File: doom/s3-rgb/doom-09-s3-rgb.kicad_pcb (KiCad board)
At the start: 4 copper layers, 182 x 80 mm, 100 parts, among them J1 54132-4062, J5 S2B-PH-K-S(LF)(SN), J6 S2B-PH-K-S(LF)(SN), Q1 AO3401A, Q2 FS8205A, SW1 PTS645SM43SMTR92 LFS, SW10 PTS645SM43SMTR92 LFS, SW11 MSK12C02, SW12 PTS645SM43SMTR92 LFS, SW13 PTS645SM43SMTR92 LFS, SW2 PTS645SM43SMTR92 LFS, SW3 PTS645SM43SMTR92 LFS, SW4 PTS645SM43SMTR92 LFS, SW5 PTS645SM43SMTR92 LFS, SW6 PTS645SM43SMTR92 LFS, SW7 PTS645SM43SMTR92 LFS, SW8 PTS645SM43SMTR92 LFS, SW9 PTS645SM43SMTR92 LFS, U1 ESP32-S3-WROOM-1-N16R8, U2 DW01A, U3 MCP23017-E/SO, U4 PCM5102APWR, U5 PAM8403DR, U6 TLV75533PDBVR, U7 BQ24075RGTR, U8 MT3608, U9 ESD 2-line

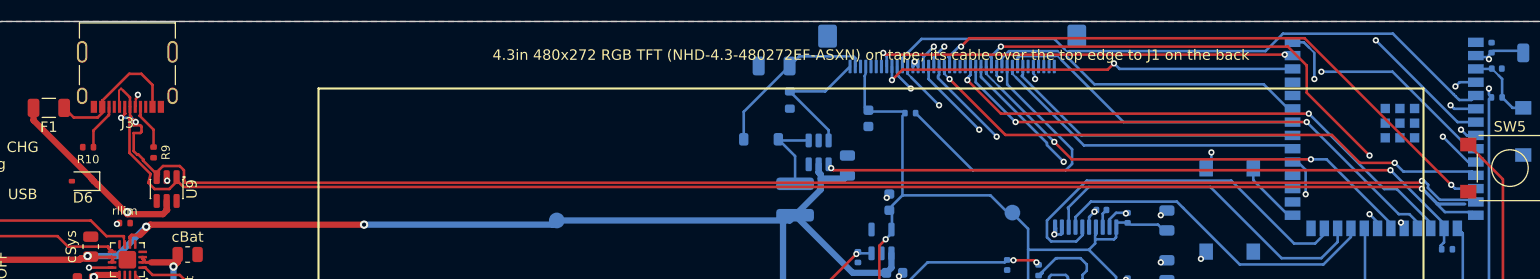
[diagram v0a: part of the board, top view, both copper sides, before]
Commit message: doom, examples: re-route around the USB-C receptacle's new land pattern
The standard receptacle became GCT USB4105's recommended layout (pcbkit 7e43c086): its shield
legs moved and two unplated guide holes appeared, under the copper these boards had been routed
with (solder-mask-bridge and clearance errors at J1). `build.run` re-routed the 3–5 nets that
crossed it: all seven check complete with 0 errors again; the six Doom boards export for the fab
without --force.

Claude-Session: https://claude.ai/code/session_01GffCzZXi9ShujPbky1eccg
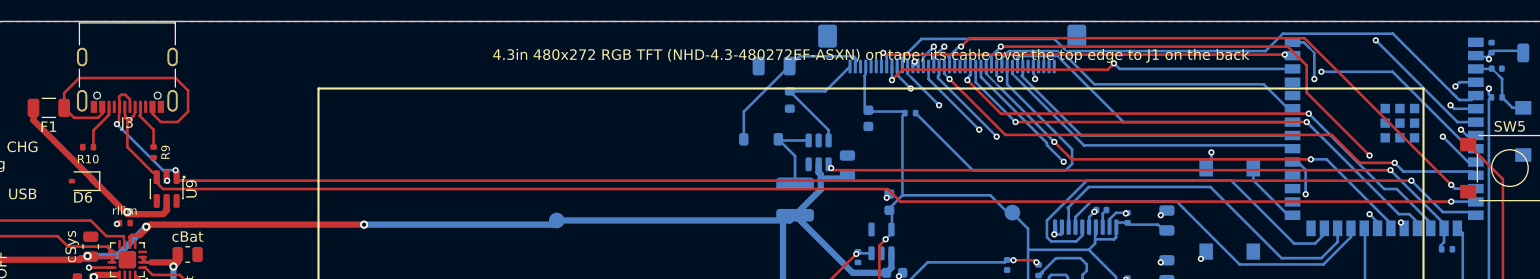
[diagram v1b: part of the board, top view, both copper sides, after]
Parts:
- removed the DS1 at (191.0, 160.0) (x4)
- added DS1 (x6): NHD-4.3-480272EF-ASXN#, Newhaven_NHD-4.3-480272EF_Panel, F.Cu at (191.0, 160.0)
- F1: value PTC 1000mA -> PTC 750mA
- J3: value (none) -> USB4105-GF-A
- U9: value ESD 2-line -> USBLC6-2SC6
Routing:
- net DP: track 149.3 -> 134.7 mm, vias 1 -> 3
- net usb/power/raw: track 14.9 -> 26.0 mm
- net DN: track 144.7 -> 133.9 mm, vias 4 -> 1

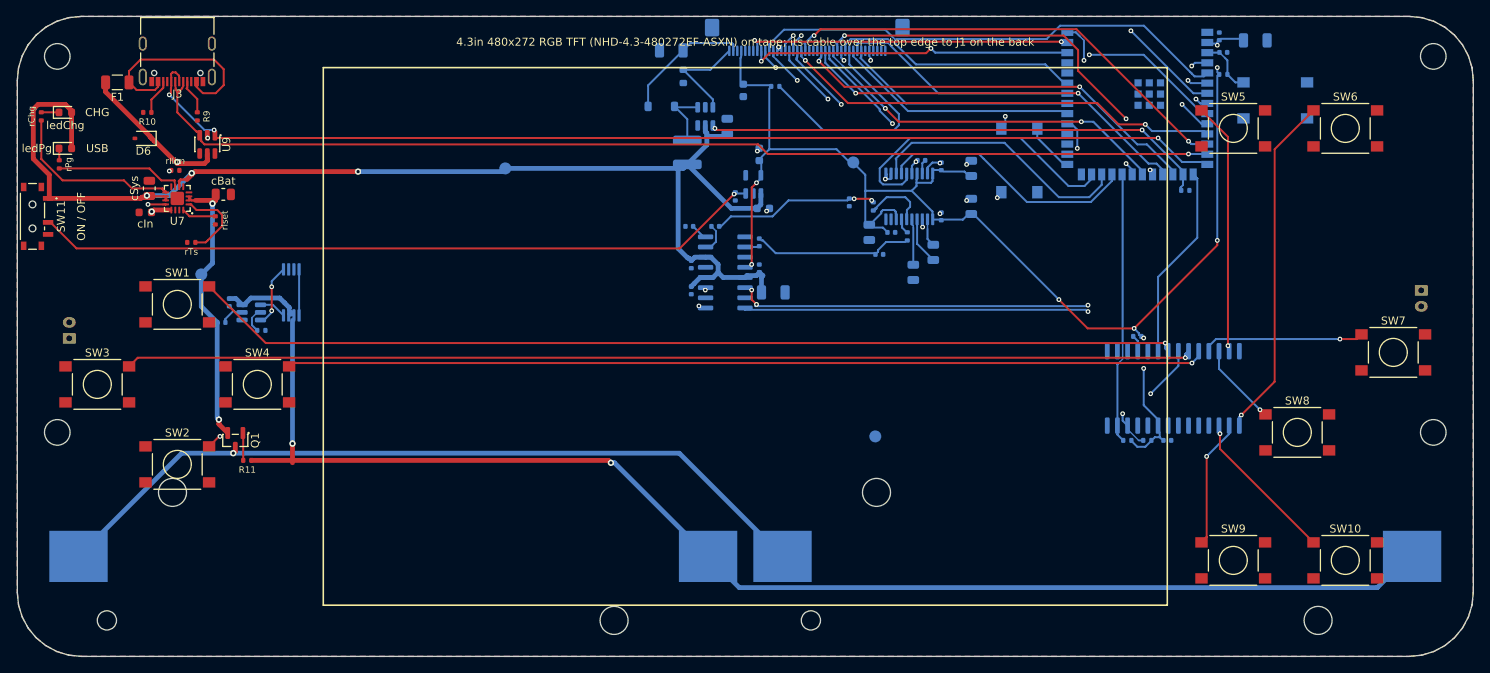
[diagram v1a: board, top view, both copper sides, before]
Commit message: doom/s3-rgb: the panel's cable reaches its connector; backlight open-LED clamp; black matte, ENIG, plated edges
The cable folded over the top edge onto the back would have arrived
contacts out, at x 105-125 mm with contact 1 on the right, 30 mm too long,
at a bottom-contact connector at x 89-108 with contact 1 on the left: the
panel could not have worked. J1 is now a Hirose FH12-40S-0.5SH (C202114)
on the front under the panel, where Newhaven's drawing folds the cable:
contacts toward the board, contact 1 at x 124.5, the slot at y 38 (the
45.7 mm cable over a 3 mm foam-tape bend reaches 33.4). Re-routed.

MT3608 has no over-voltage protection: with no panel plugged in, FB sat at
0 V and the boost would climb past its 30 V switch. A 28 V zener
(MMSZ5255B, C3031843) into FB through 1 kOhm clamps it; the panel's
strings (22.4-27.2 V) stay below.

check: complete, 0 errors (USB pair now 129 mm coupled); ready: nothing
to fix; fab export without --force.

Claude-Session: https://claude.ai/code/session_01EdwxjCrDS3n9c3uBXz6P7n
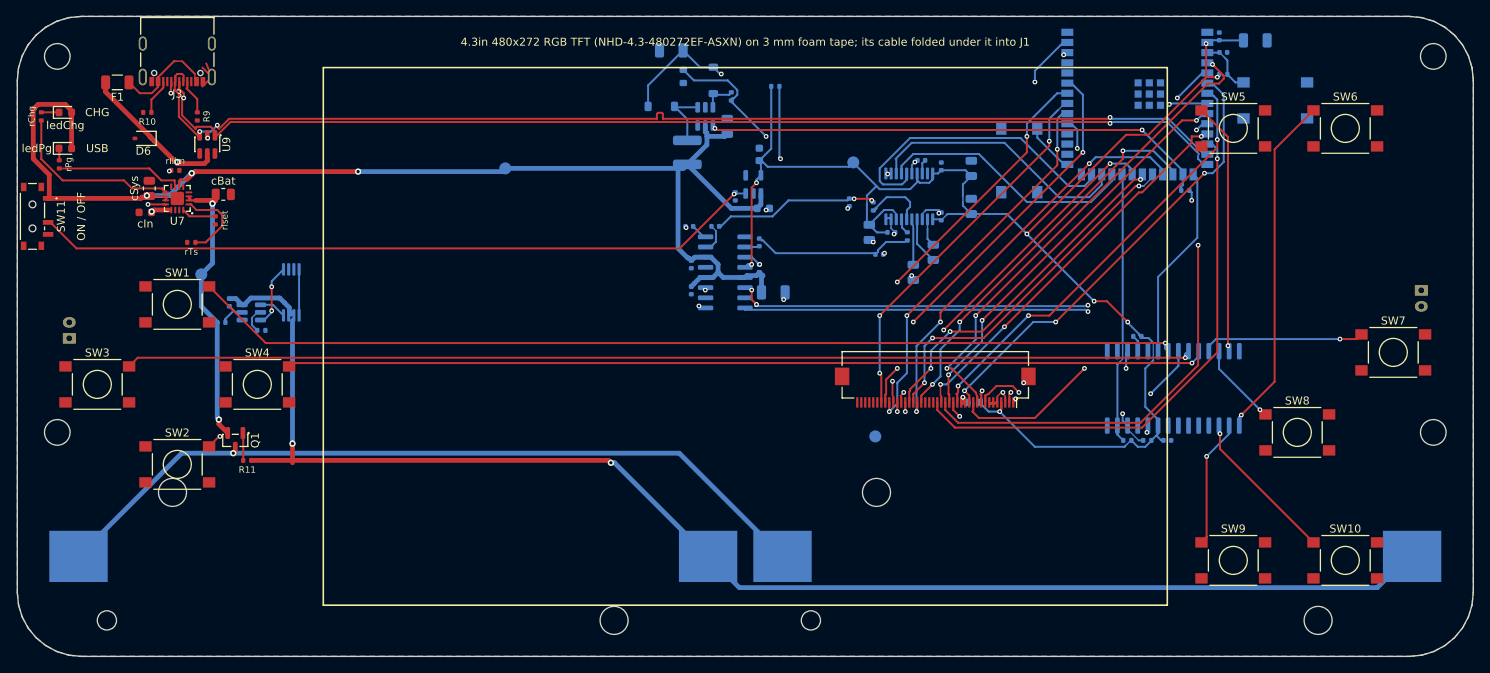
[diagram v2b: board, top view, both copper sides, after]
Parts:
- removed the DS1 at (191.0, 160.0) (x6)
- added D2: zener 28V, D_SOD-123, B.Cu at (187.0, 128.0)
- added DS1 (x11): NHD-4.3-480272EF-ASXN#, Newhaven_NHD-4.3-480272EF_Panel, F.Cu at (191.0, 160.0)
- added R15: 1kohm, R_0402_1005Metric, B.Cu at (189.2, 130.0)
- J1: value 54132-4062 -> FH12-40S-0.5SH(55); footprint Conn_FFC-FPC_1x40_P0.50mm_Horizontal -> Connector_FFC-FPC:Hirose_FH12-40S-0.5SH_1x40-1MP_P0.50mm_Horizontal; moved to F.Cu
- moved C1 48.5 mm to (219.5, 168.2), turned to 0 degrees
- moved J1 45.0 mm to (214.8, 166.4)
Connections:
- U8 pad 3: LED_K -> BL_FB
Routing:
- net LED_A: track 16.3 -> 70.9 mm, vias 0 -> 2
- net V3: track 155.9 -> 207.1 mm, vias 9 -> 8
- net LED_K: track 13.0 -> 63.4 mm, vias 0 -> 2
- net PCLK: track 31.1 -> 52.9 mm, vias 0 -> 3
- net VSYNC: track 29.7 -> 48.8 mm, vias 0 -> 3
- net DE: track 29.1 -> 47.4 mm, vias 0 -> 3
- net HSYNC: track 31.8 -> 48.0 mm, vias 0 -> 3
- net DISP: track 29.3 -> 45.4 mm, vias 0 -> 2
- net usb/power/raw: track 26.0 -> 12.9 mm
- net RED3: track 39.8 -> 52.6 mm
- net RED4: track 40.4 -> 52.9 mm
- net GRN5: track 56.0 -> 67.5 mm
- net GND: track 19.2 -> 29.8 mm, vias 16 -> 20
- net GRN7: track 58.0 -> 67.7 mm, vias 2 -> 1
- net GRN3: track 55.7 -> 64.9 mm
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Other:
- board text added: "4.3in 480x272 RGB TFT (NHD-4.3-480272EF-ASXN) on 3 mm foam tape; its cable folded under it into J1"
- board text removed: "4.3in 480x272 RGB TFT (NHD-4.3-480272EF-ASXN) on tape; its cable over the top edge to J1 on the back"

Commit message: doom/s3-rgb: SMD speakers assembled on the back; the brand on the front, no refdes there
The two speakers on JST plugs had to be bought and wired by hand: two
FS-1540 15 x 15 mm SMD speakers (8 ohm, 0.5 W, C482341) now sit on the
back at the two ends and JLCPCB places them. 100 kOhm before each PAM8403
input lowers its gain to 1.6 dB so the DAC's full scale stays within the
speakers' 0.8 W maximum.

The front loses the long panel note and every reference designator (the
back keeps them); the PCBKit mark sits under the D-pad and pcbkit.io
between the right-hand buttons (both cut from the logo part).

check: complete, 0 errors; ready: nothing to fix; fab export clean.

Claude-Session: https://claude.ai/code/session_01EdwxjCrDS3n9c3uBXz6P7n
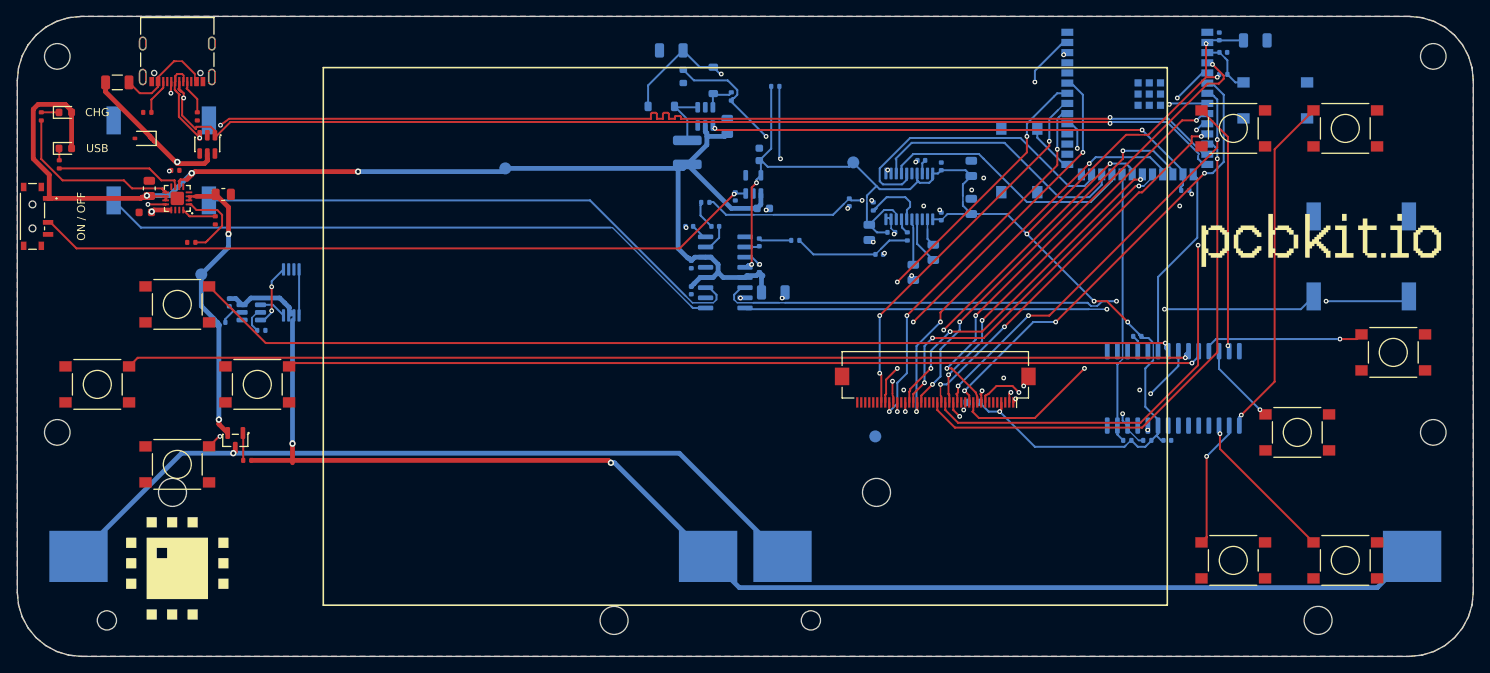
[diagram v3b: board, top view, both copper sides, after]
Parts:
- removed the DS1 at (191.0, 160.0) (x11)
- removed J5, J6: S2B-PH-K-S(LF)(SN), JST_PH_S2B-PH-K_1x02_P2.00mm_Horizontal
- added DS1 (x18): NHD-4.3-480272EF-ASXN#, Newhaven_NHD-4.3-480272EF_Panel, F.Cu at (191.0, 160.0)
- added LS1: FS-1540, Speaker_FUET_FS-1540_15x15mm, B.Cu at (118.0, 138.0)
- added LS2: FS-1540, Speaker_FUET_FS-1540_15x15mm, B.Cu at (268.0, 150.0)
- added R16: 100kohm, R_0402_1005Metric, B.Cu at (186.0, 143.2)
- added R17: 100kohm, R_0402_1005Metric, B.Cu at (197.2, 148.0)
- added mark: , Logo_PCBKit_mark, F.Cu at (120.0, 189.0)
- added wordmark: , Logo_PCBKit_wordmark, F.Cu at (263.0, 148.0)
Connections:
- C24 pad 1: LINE_L -> Net-(C24-1)
- C24 pad 2: Net-(C24-1) -> AMP_L
- C25 pad 2: LINE_R -> AMP_R
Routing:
- net GND: track 29.8 -> 6.07 mm, vias 20 -> 24
- net SPK_RP: track 90.1 -> 71.8 mm, vias 1 -> 2
- net SPK_LN: track 83.7 -> 71.3 mm, vias 1 -> 0
- net SPK_LP: track 83.8 -> 79.6 mm, vias 1 -> 0
- net AMP_R: track 0.00 -> 4.09 mm
- net LINE_R: track 19.0 -> 14.9 mm
- net AMP_L: track 0.00 -> 3.60 mm
- net BAT: track 35.2 -> 37.9 mm
- net DN: track 141.4 -> 143.4 mm
- net LINE_L: track 20.6 -> 21.9 mm
- net SPK_RN: track 87.2 -> 87.5 mm, vias 3 -> 2
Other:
- board text removed: "4.3in 480x272 RGB TFT (NHD-4.3-480272EF-ASXN) on 3 mm foam tape; its cable folded under it into J1"

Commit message: doom/s3-rgb: the ASXP panel (the ASXN is discontinued); a connector with top and bottom contacts
Newhaven discontinued the NHD-4.3-480272EF-ASXN; the NHD-4.3-480272EF-ASXP
(IPS, in stock at DigiKey and Mouser) has the same outline, cable and
pinout, but its SC7283 wants HSYNC/VSYNC pulses of 2+ clocks and a 55-65 us
line: the firmware now drives its typical timing (8.9 MHz, 4 + 39 + 480 + 8,
4 + 8 + 272 + 8: 57 Hz) instead of 10 MHz, 1-clock pulses and 52.6 us.
Newhaven names a bottom-contact connector for one and a top-contact one for
the other: J1 is now a Hirose FH34SRJ-40S-0.5SH(50) (C506798) with contacts
on both sides, 1 mm high, contact 1 still at x 124.5 where the folded cable
brings it.

check: complete, 0 errors; ready: nothing to fix; firmware compiles as in
the browser (121 files, 7.6 s).

Claude-Session: https://claude.ai/code/session_01EdwxjCrDS3n9c3uBXz6P7n
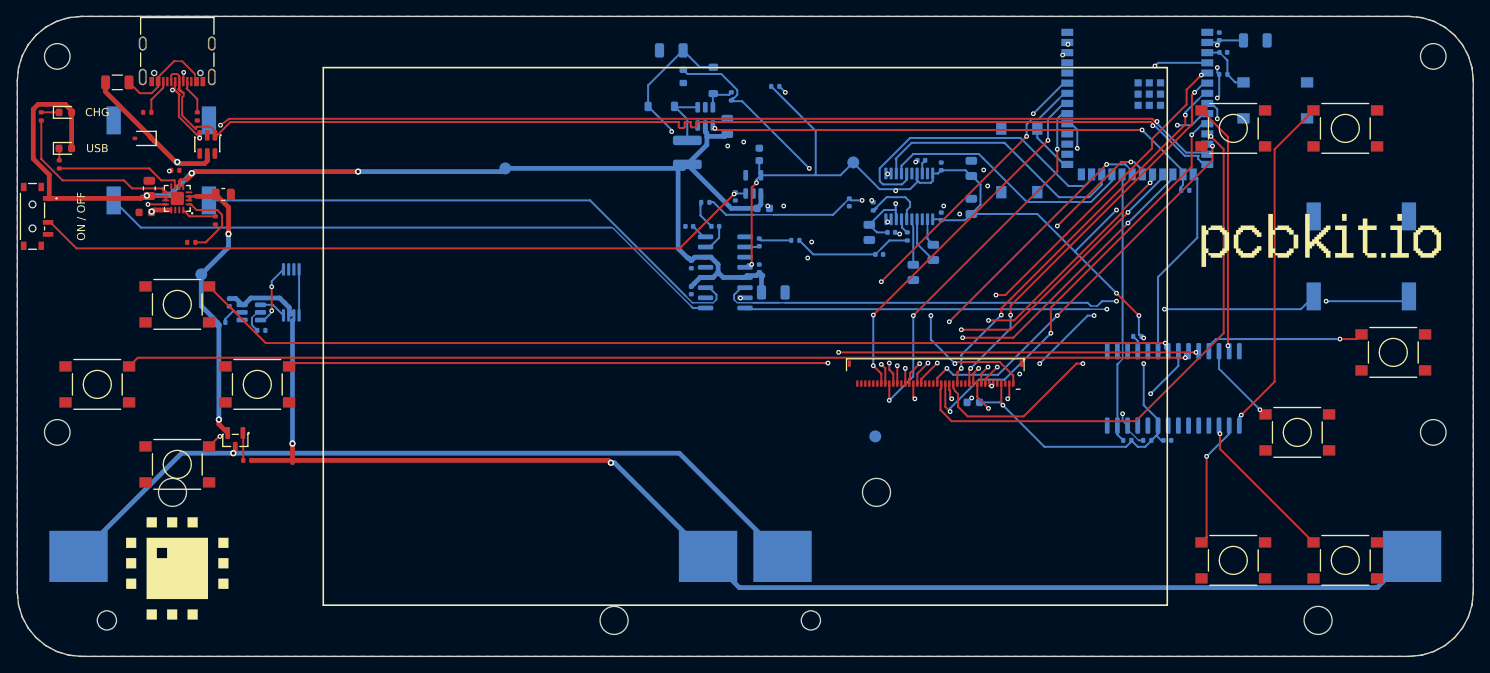
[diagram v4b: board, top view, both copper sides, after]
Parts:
- removed the DS1 at (191.0, 160.0) (x18)
- added DS1 (x18): NHD-4.3-480272EF-ASXN#, Newhaven_NHD-4.3-480272EF_Panel, F.Cu at (191.0, 160.0)
- added DS1 (x6): NHD-4.3-480272EF-ASXP, Newhaven_NHD-4.3-480272EF_Panel, F.Cu at (191.0, 160.0)
- J1: value FH12-40S-0.5SH(55) -> FH34SRJ-40S-0.5SH(50); footprint Connector_FFC-FPC:Hirose_FH12-40S-0.5SH_1x40-1MP_P0.50mm_Horizontal -> Hirose_FH34SRJ-40S-0.5SH_1x40-1MP_P0.50mm_Horizontal
- moved J1 0.50 mm to (214.8, 165.9), turned to 0 degrees
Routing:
- net GRN6: track 48.2 -> 69.1 mm, vias 3 -> 1
- net GRN7: track 67.7 -> 48.8 mm, vias 1 -> 3
- net V3: track 207.1 -> 192.7 mm, vias 8 -> 13
- net GRN5: track 67.5 -> 55.3 mm, vias 2 -> 3
- net RED6: track 61.9 -> 51.1 mm, vias 2 -> 3
- net BLU4: track 51.9 -> 42.5 mm
- net LED_A: track 70.9 -> 79.2 mm
- net RED4: track 52.9 -> 45.3 mm
- net RED7: track 57.0 -> 50.1 mm
- net BLU3: track 49.7 -> 42.9 mm
- net PCLK: track 52.9 -> 46.6 mm, vias 3 -> 2
- net GND: track 6.07 -> 0.00 mm, vias 24 -> 18
- net RED3: track 52.6 -> 46.7 mm
- net GRN4: track 50.9 -> 56.6 mm, vias 3 -> 4
- net GRN2: track 54.5 -> 49.4 mm
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
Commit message: doom/s3-rgb: the picture the right way up on the panel as it is taped on
The panel lies with its cable side (the bottom of its scan) at the board's top edge, half a turn
from its drawing, and the firmware sent frames as is: the game would show upside down. The frame
now goes out from its last pixel to its first, and DS1 turns 180° so the laboratory shows the panel
as built. The .kicad_pcb keeps one DS1 instead of 24 (pcbkit cb68f6ff); its Gerbers, drills, BOM
and placement are byte for byte the ones ordered. check: complete; firmware compiles (121 files).

Claude-Session: https://claude.ai/code/session_01EdwxjCrDS3n9c3uBXz6P7n
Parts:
- removed the DS1 at (191.0, 160.0) (x24)
- added DS1: NHD-4.3-480272EF-ASXP, Newhaven_NHD-4.3-480272EF_Panel, F.Cu at (191.0, 160.0)
